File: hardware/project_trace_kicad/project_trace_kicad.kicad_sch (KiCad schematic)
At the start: 0 parts

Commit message: Before Changes to Input Section
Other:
- sheet Data Acquisition: AC renamed ADC
- removed sheet Data Acquisition: DC
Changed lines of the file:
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@@
-	)
-	(sheet
-		(at 95.25 50.8)
-		(size 38.1 12.7)
-		(exclude_from_sim no)
-		(in_bom yes)
-		(on_board yes)
-		(dnp no)
-		(fields_autoplaced yes)
-		(stroke
-			(width 0.1524)
-			(type solid)
-			(color 0 0 0 0.6)
-		)
-		(fill
-			(color 215 236 255 1.0000)
-		)
-		(property "Sheetname" "Data Acquisition: DC"
-			(at 95.25 50.0884 0)
-			(effects
-				(font
-					(size 1.27 1.27)
-				)
-				(justify left bottom)
-			)
-		)
-		(property "Sheetfile" "DAQ_DC.kicad_sch"
-			(at 95.25 64.0846 0)
-			(effects
-				(font
-					(size 1.27 1.27)
-				)
-				(justify left top)
-			)
-		)
-		(instances
-			(project "project_trace_kicad"
-				(path "/af51f4e5-b952-4b0e-baf2-78a72fb86fcd"
-					(page "4")
-				)
-			)
-		)
 	)
 	(sheet
@@
 			(color 215 236 255 1.0000)
 		)
-		(property "Sheetname" "Data Acquisition: AC"
+		(property "Sheetname" "ADC"
 			(at 95.25 81.8384 0)
 			(effects

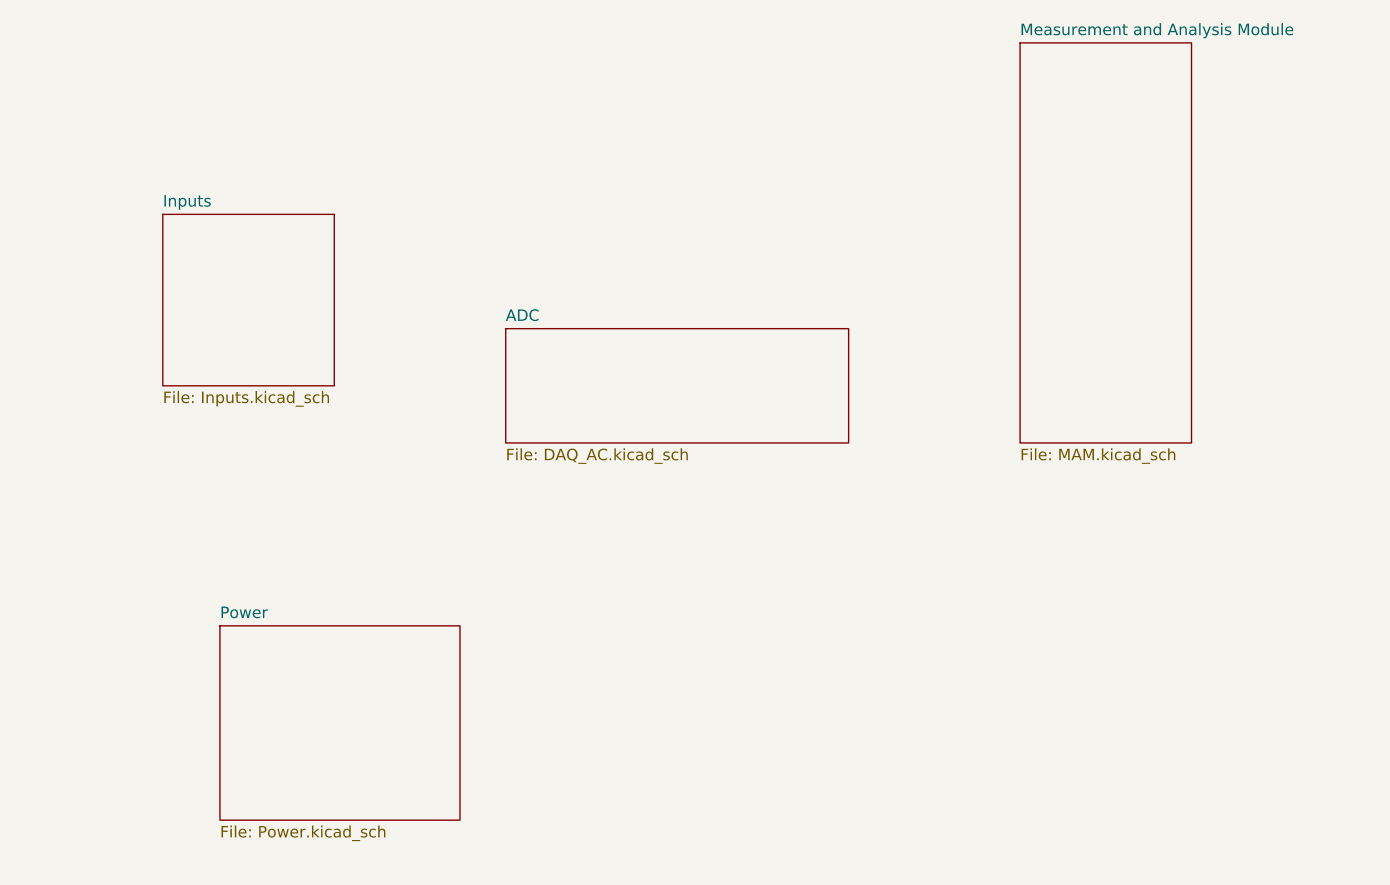
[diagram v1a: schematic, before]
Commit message: Change designators, Improve Input Circuit
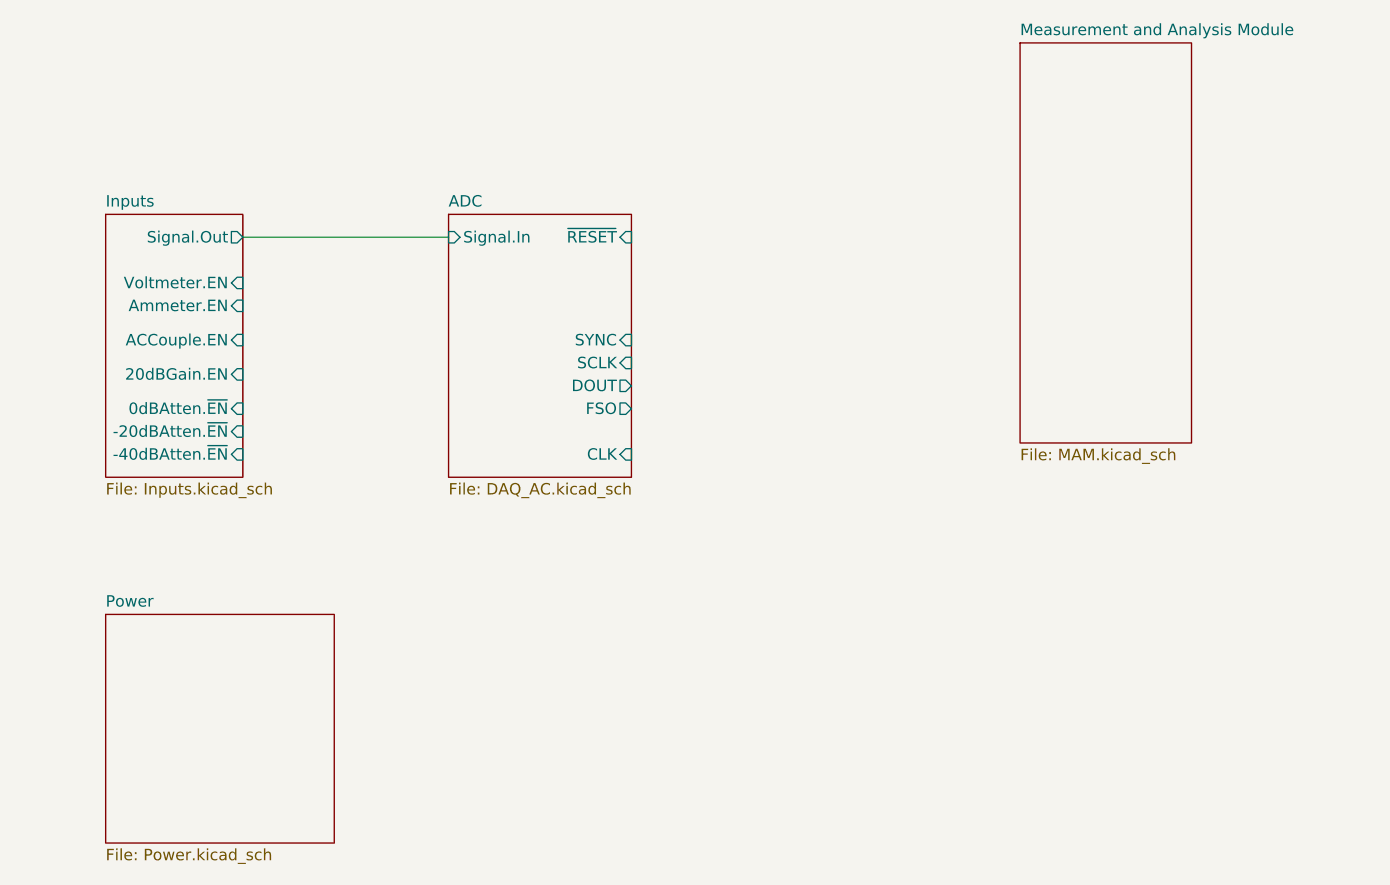
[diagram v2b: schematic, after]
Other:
- sheet ADC ports: added CLK, DOUT, FSO, SCLK, SYNC, Signal.In, ~{RESET}; removed none
- sheet Inputs ports: added -20dBAtten.~{EN}, -40dBAtten.~{EN}, 0dBAtten.~{EN}, 20dBGain.EN, ACCouple.EN, Ammeter.EN, Signal.Out, Voltmeter.EN; removed none
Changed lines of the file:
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@@
 	(generator_version "9.0")
 	(paper "A4")
+	(wire
+		(pts
+			(xy 66.04 72.39) (xy 88.9 72.39)
+		)
+		(stroke
+			(width 0)
+			(type default)
+		)
+	)
 	(sheet
-		(at 63.5 115.57)
-		(size 26.67 21.59)
+		(at 50.8 114.3)
+		(size 25.4 25.4)
 		(exclude_from_sim no)
 		(in_bom yes)
@@
 		)
 		(property "Sheetname" "Power"
-			(at 63.5 114.8584 0)
+			(at 50.8 113.5884 0)
 			(effects
 				(font
@@
 		)
 		(property "Sheetfile" "Power.kicad_sch"
-			(at 63.5 137.7446 0)
+			(at 50.8 140.2846 0)
 			(effects
 				(font
@@
 	)
 	(sheet
-		(at 57.15 69.85)
-		(size 19.05 19.05)
+		(at 50.8 69.85)
+		(size 15.24 29.21)
 		(exclude_from_sim no)
 		(in_bom yes)
@@
 		)
 		(property "Sheetname" "Inputs"
-			(at 57.15 69.1384 0)
+			(at 50.8 69.1384 0)
 			(effects
 				(font
@@
 		)
 		(property "Sheetfile" "Inputs.kicad_sch"
-			(at 57.15 89.4846 0)
+			(at 50.8 99.6446 0)
 			(effects
 				(font
@@
 				)
 				(justify left top)
+			)
+		)
+		(pin "ACCouple.EN" input
+			(at 66.04 83.82 0)
+			(effects
+				(font
+					(size 1.27 1.27)
+				)
+				(justify right)
+			)
+		)
+		(pin "Ammeter.EN" input
+			(at 66.04 80.01 0)
+			(effects
+				(font
+					(size 1.27 1.27)
+				)
+				(justify right)
+			)
+		)
+		(pin "Voltmeter.EN" input
+			(at 66.04 77.47 0)
+			(effects
+				(font
+					(size 1.27 1.27)
+				)
+				(justify right)
+			)
+		)
+		(pin "-20dBAtten.~{EN}" input
+			(at 66.04 93.98 0)
+			(effects
+				(font
+					(size 1.27 1.27)
+				)
+				(justify right)
+			)
+		)
+		(pin "-40dBAtten.~{EN}" input
+			(at 66.04 96.52 0)
+			(effects
+				(font
+					(size 1.27 1.27)
+				)
+				(justify right)
+			)
+		)
+		(pin "0dBAtten.~{EN}" input
+			(at 66.04 91.44 0)
+			(effects
+				(font
+					(size 1.27 1.27)
+				)
+				(justify right)
+			)
+		)
+		(pin "20dBGain.EN" input
+			(at 66.04 87.63 0)
+			(effects
+				(font
+					(size 1.27 1.27)
+				)
+				(justify right)
+			)
+		)
+		(pin "Signal.Out" output
+			(at 66.04 72.39 0)
+			(effects
+				(font
+					(size 1.27 1.27)
+				)
+				(justify right)
 			)
 		)
@@
 	)
 	(sheet
-		(at 95.25 82.55)
-		(size 38.1 12.7)
+		(at 88.9 69.85)
+		(size 20.32 29.21)
 		(exclude_from_sim no)
 		(in_bom yes)
@@
 		)
 		(property "Sheetname" "ADC"
-			(at 95.25 81.8384 0)
+			(at 88.9 69.1384 0)
 			(effects
 				(font
@@
 		)
 		(property "Sheetfile" "DAQ_AC.kicad_sch"
-			(at 95.25 95.8346 0)
+			(at 88.9 99.6446 0)
 			(effects
 				(font
@@
 			)
 		)
+		(pin "CLK" input
+			(at 109.22 96.52 0)
+			(effects
+				(font
+					(size 1.27 1.27)
+				)
+				(justify right)
+			)
+		)
+		(pin "DOUT" output
+			(at 109.22 88.9 0)
+			(effects
+				(font
+					(size 1.27 1.27)
+				)
+				(justify right)
+			)
+		)
+		(pin "FSO" output
+			(at 109.22 91.44 0)
+			(effects
+				(font
+					(size 1.27 1.27)
+				)
+				(justify right)
+			)
+		)
+		(pin "SCLK" input
+			(at 109.22 86.36 0)
+			(effects
+				(font
+					(size 1.27 1.27)
+				)
+				(justify right)
+			)
+		)
+		(pin "Signal.In" input
+			(at 88.9 72.39 180)
+			(effects
+				(font
+					(size 1.27 1.27)
+				)
+				(justify left)
+			)
+		)
+		(pin "SYNC" input
+			(at 109.22 83.82 0)
+			(effects
+				(font
+					(size 1.27 1.27)
+				)
+				(justify right)
+			)
+		)
+		(pin "~{RESET}" input
+			(at 109.22 72.39 0)
+			(effects
+				(font
+					(size 1.27 1.27)
+				)
+				(justify right)
+			)
+		)

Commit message: Improve Inputs, Source Parts, Add Credits
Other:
- title: (none) -> Multilloscope
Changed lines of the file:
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@@
 	(generator_version "9.0")
 	(paper "A4")
+	(title_block
+		(title "Multilloscope")
+		(comment 1 "Marius H. Tyson")
+		(comment 2 "Alexander N. Olsen")
+		(comment 3 "Laurits K. Hillemann")
+	)
 	(wire
 		(pts

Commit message: Lotsa Changes
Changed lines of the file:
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@@
 (kicad_sch
-	(version 20250114)
+	(version 20260306)
 	(generator "eeschema")
-	(generator_version "9.0")
+	(generator_version "10.0")
 	(paper "A4")
 	(title_block
@@
 	(wire
 		(pts
-			(xy 66.04 72.39) (xy 88.9 72.39)
+			(xy 63.5 72.39) (xy 88.9 72.39)
 		)
 		(stroke
@@
 		)
 		(fill
-			(color 0 0 0 0.0000)
+			(color 0 0 0 0)
 		)
 		(property "Sheetname" "Power"
 			(at 50.8 113.5884 0)
+			(show_name no)
+			(do_not_autoplace no)
 			(effects
 				(font
@@
 		(property "Sheetfile" "Power.kicad_sch"
 			(at 50.8 140.2846 0)
+			(show_name no)
+			(do_not_autoplace no)
 			(effects
 				(font
@@
 	)
 	(sheet
-		(at 50.8 69.85)
-		(size 15.24 29.21)
+		(at 44.45 69.85)
+		(size 19.05 29.21)
 		(exclude_from_sim no)
 		(in_bom yes)
@@
 			(width 0.1524)
 			(type solid)
-			(color 0 0 0 0.6)
 		)
 		(fill
-			(color 215 236 255 1.0000)
+			(color 0 0 0 0)
 		)
 		(property "Sheetname" "Inputs"
-			(at 50.8 69.1384 0)
+			(at 44.45 69.1384 0)
+			(show_name no)
+			(do_not_autoplace no)
 			(effects
 				(font
@@
 		)
 		(property "Sheetfile" "Inputs.kicad_sch"
-			(at 50.8 99.6446 0)
+			(at 44.45 99.6446 0)
+			(show_name no)
+			(do_not_autoplace no)
 			(effects
 				(font
@@
 		)
 		(pin "ACCouple.EN" input
-			(at 66.04 83.82 0)
+			(at 63.5 83.82 0)
 			(effects
 				(font
@@
 		)
 		(pin "Ammeter.EN" input
-			(at 66.04 80.01 0)
+			(at 63.5 80.01 0)
 			(effects
 				(font
@@
 		)
 		(pin "Voltmeter.EN" input
-			(at 66.04 77.47 0)
+			(at 63.5 77.47 0)
 			(effects
 				(font
@@
 		)
 		(pin "-20dBAtten.~{EN}" input
-			(at 66.04 93.98 0)
+			(at 63.5 93.98 0)
 			(effects
 				(font
@@
 		)
 		(pin "-40dBAtten.~{EN}" input
-			(at 66.04 96.52 0)
+			(at 63.5 96.52 0)
 			(effects
 				(font
@@
 		)
 		(pin "0dBAtten.~{EN}" input
-			(at 66.04 91.44 0)
+			(at 63.5 91.44 0)
 			(effects
 				(font
@@
 		)
 		(pin "20dBGain.EN" input
-			(at 66.04 87.63 0)
+			(at 63.5 87.63 0)
 			(effects
 				(font
@@
 		)
 		(pin "Signal.Out" output
-			(at 66.04 72.39 0)
+			(at 63.5 72.39 0)
 			(effects
 				(font
@@
 	(sheet
 		(at 88.9 69.85)
-		(size 20.32 29.21)
+		(size 20.32 22.225)
 		(exclude_from_sim no)
 		(in_bom yes)
@@
 			(width 0.1524)
 			(type solid)
-			(color 0 0 0 0.6)
 		)
 		(fill
-			(color 215 236 255 1.0000)
+			(color 0 0 0 0)
 		)
 		(property "Sheetname" "ADC"
 			(at 88.9 69.1384 0)
+			(show_name no)
+			(do_not_autoplace no)
 			(effects
 				(font
@@
 		)
 		(property "Sheetfile" "DAQ_AC.kicad_sch"
-			(at 88.9 99.6446 0)
+			(at 88.9 92.6596 0)
+			(show_name no)
+			(do_not_autoplace no)
 			(effects
 				(font
@@
 		)
 		(pin "CLK" input
-			(at 109.22 96.52 0)
+			(at 109.22 90.17 0)
 			(effects
 				(font
@@
 		)
 		(pin "DOUT" output
-			(at 109.22 88.9 0)
+			(at 109.22 82.55 0)
 			(effects
 				(font
@@
 		)
 		(pin "FSO" output
-			(at 109.22 91.44 0)
+			(at 109.22 85.09 0)
 			(effects
 				(font
@@
 		)
 		(pin "SCLK" input
-			(at 109.22 86.36 0)
+			(at 109.22 80.01 0)
 			(effects
 				(font
@@
 		)
 		(pin "SYNC" input
-			(at 109.22 83.82 0)
+			(at 109.22 77.47 0)
 			(effects
 				(font
@@
 			(width 0.1524)
 			(type solid)
-			(color 0 0 0 0.6)
 		)
 		(fill
-			(color 215 236 255 1.0000)
+			(color 0 0 0 0)
 		)
 		(property "Sheetname" "Measurement and Analysis Module"
 			(at 152.4 50.0884 0)
+			(show_name no)
+			(do_not_autoplace no)
 			(effects
 				(font
@@
 		(property "Sheetfile" "MAM.kicad_sch"
 			(at 152.4 95.8346 0)
-			(effects
-				(font
+			(show_name no)
+			(do_not_autoplace no)
+			(effects
+				(font
